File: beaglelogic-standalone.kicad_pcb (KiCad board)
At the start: 4 copper layers, 247 parts, among them J1 USB_OTG, J2 CONN_02X02, J3 USB_A, J4 CONN_01X06, J5 SI-51009-F, J6 CONN_02X12, J7 CONN_02X16, Q1 BSS138, Q2 BSS138, SW1 SW_PUSH_SMALL_H, SW2 SW_PUSH_SMALL_H, U1 74LVC1G07, U10 MCP79410/TDFN, U11 SST26VF064B, U12 TPS73101, U13 SN74LVCH16T245, U14 DVIULC6-4SC6, U15 DVIULC6-4SC6, U16 DVIULC6-4SC6, U17 DVIULC6-4SC6, U18 74LV1T125, U19 EMMC_4G, U2 AP1117, U3 TPS2051C, U4 TPD4S012, U5 TPD4S012, U6 OSD3358-SM, U7 KSZ9031RNXCC, U8 74LVC2G241, U9 74LVC1G125, Y1 25MHz, Y2 24MHz, Y3 32.768kHz,CL=9pF

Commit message: More routing
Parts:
- C44, C45, C46, C47, C48, C49, C50, C51, C54, C55, C56, C57, C58, C59, C60, C61, R103, R104, R105, R106, R107, R108, R109, R110, R111, R112, R113, R114, R115, R116, R117, R118, R119, R120, R121, R122, R123, R124, R125, R126, R42, R43, R65, R66, R67, R68, R69, R70, R71, R72, R73, R74, R75, R76, R77, R78, R79, R80, R87, R88, R89, R90, R91, R92, R93, R94, TP2, TP4, TP5, U13, U14, U15, U16, U17, U5: moved to B.Cu
- JP1, R46: moved to F.Cu
- moved R46 56.0 mm to (65.6, 147.6), turned to 270 degrees
- moved R45 54.1 mm to (57.5, 150.9), turned to 180 degrees
- moved R44 51.5 mm to (57.5, 149.7)
- moved JP1 51.2 mm to (54.1, 144.8)
- moved C36 50.7 mm to (58.0, 143.5)
- moved U11 49.1 mm to (65.0, 143.8), turned to 180 degrees
- moved C38 48.0 mm to (64.7, 140.4)
- moved U9 47.0 mm to (63.4, 148.1)
- moved C34 40.6 mm to (114.5, 128.7)
- moved C35 40.6 mm to (114.5, 130.8)
- moved Y3 40.4 mm to (116.4, 129.7)
- moved C37 40.1 mm to (119.5, 128.2)
- moved R47 40.1 mm to (121.8, 129.7)
- moved U10 40.1 mm to (119.5, 130.5)
- moved BT1 37.9 mm to (116.1, 134.0), turned to 0 degrees
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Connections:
- RN1 pad 1: +3V3 -> Net-(RN1-Pad1)
- RN1 pad 2: +3V3 -> /PRU1_IN05
- RN1 pad 3: +3V3 -> /PRU1_IN04
- RN1 pad 4: +3V3 -> /PRU1_IN03
- RN1 pad 5: /PRU1_IN03 -> +3V3
- RN1 pad 6: /PRU1_IN04 -> +3V3
- RN1 pad 7: /PRU1_IN05 -> +3V3
- RN1 pad 8: Net-(RN1-Pad8) -> +3V3
- U13 pad 11: /DIN09 -> /DIN06
- U13 pad 12: /DIN08 -> /DIN07
- U13 pad 13: /DIN07 -> /DIN08
- U13 pad 14: /DIN06 -> /DIN09
- U13 pad 16: /DIN05 -> /DIN10
- U13 pad 17: /DIN04 -> /DIN11
- U13 pad 19: /DIN03 -> /DIN12
- U13 pad 2: /DIN15 -> /DIN00
- U13 pad 20: /DIN02 -> /DIN13
- U13 pad 22: /DIN01 -> /DIN14
- U13 pad 23: /DIN00 -> /DIN15
- U13 pad 26: /PRU1_IN00 -> /PRU1_IN15
- U13 pad 27: /PRU1_IN01 -> /PRU1_IN14
- U13 pad 29: /PRU1_IN02 -> /PRU1_IN13
- U13 pad 3: /DIN14 -> /DIN01
- U13 pad 30: /PRU1_IN03 -> /PRU1_IN12
- U13 pad 32: /PRU1_IN04 -> /PRU1_IN11
- U13 pad 33: /PRU1_IN05 -> /PRU1_IN10
- U13 pad 35: /PRU1_IN06 -> /PRU1_IN09
- U13 pad 36: /PRU1_IN07 -> /PRU1_IN08
- U13 pad 37: /PRU1_IN08 -> /PRU1_IN07
- U13 pad 38: /PRU1_IN09 -> /PRU1_IN06
- U13 pad 40: /PRU1_IN10 -> /PRU1_IN05
- U13 pad 41: /PRU1_IN11 -> /PRU1_IN04
- U13 pad 43: /PRU1_IN12 -> /PRU1_IN03
- U13 pad 44: /PRU1_IN13 -> /PRU1_IN02
- U13 pad 46: /PRU1_IN14 -> /PRU1_IN01
- U13 pad 47: /PRU1_IN15 -> /PRU1_IN00
- U13 pad 5: /DIN13 -> /DIN02
- U13 pad 6: /DIN12 -> /DIN03
- U13 pad 8: /DIN11 -> /DIN04
- U13 pad 9: /DIN10 -> /DIN05
- U6 pad L1: Net-(RN1-Pad8) -> Net-(RN1-Pad1)
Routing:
- net /TRD4+: track 16.0 -> 0.00 mm
- net /TRD4-: track 15.9 -> 0.00 mm
- net USB0_D+: track 36.9 -> 21.1 mm
- net /TRD3+: track 14.7 -> 0.00 mm
- net /TRD3-: track 14.6 -> 0.00 mm
- net /TRD1+: track 14.5 -> 0.00 mm
- net /TRD1-: track 14.5 -> 0.00 mm
- net /TRD2+: track 13.9 -> 0.00 mm
- net /TRD2-: track 13.9 -> 0.00 mm
- net Net-(C11-Pad1): track 0.00 -> 13.3 mm, vias 0 -> 3
- net Net-(C12-Pad1): track 18.3 -> 28.6 mm, vias 5 -> 6
- net USB1_D-: track 30.7 -> 20.6 mm
- net USB1_D+: track 32.2 -> 22.2 mm
- net USB0_D-: track 36.9 -> 27.0 mm
- net Net-(C25-Pad1): track 0.00 -> 7.80 mm
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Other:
- board outline added: 106.4 x 66.1 mm

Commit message: Update routing and schematic
Signed-off-by: Kumar Abhishek <abhishek@theembeddedkitchen.net>
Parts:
- removed TP1: 5V, Measurement_Points:Measurement_Point_Round-SMD-Pad_Small
- added J8: Barrel_Jack, Connect:BARREL_JACK, F.Cu at (103.2, 123.9)
- added LOGO1: TEST_1P, beaglelogic-standalone:beaglelogic-logo, F.Cu at (106.6, 132.6)
- added M1: TEST_1P, Mounting_Holes:MountingHole_3.2mm_M3, F.Cu at (22.0, 166.4)
- added M2: TEST_1P, Mounting_Holes:MountingHole_3.2mm_M3, F.Cu at (123.1, 165.4)
- added M3: TEST_1P, Mounting_Holes:MountingHole_3.2mm_M3, F.Cu at (23.5, 106.7)
- added M4: TEST_1P, Mounting_Holes:MountingHole_3.2mm_M3, F.Cu at (120.9, 108.2)
- C40, C41, U14, U15, U16, U17: moved to F.Cu
- C43, C52, R81, R82, R95, U18: moved to B.Cu
- moved Y3 91.0 mm to (31.1, 161.5)
- moved BT1 91.0 mm to (30.8, 165.8)
- moved C34 91.0 mm to (29.2, 160.4)
- moved C35 91.0 mm to (29.2, 162.6)
- moved C37 91.0 mm to (34.2, 160.0)
- moved R47 91.0 mm to (36.5, 161.5)
- moved U10 91.0 mm to (34.2, 162.3)
- moved C41 16.6 mm to (24.3, 160.6), turned to 270 degrees
- moved C40 16.2 mm to (25.6, 160.7), turned to 270 degrees
- moved Q1 15.3 mm to (108.1, 139.9)
- moved C39 11.1 mm to (91.0, 141.5)
- moved R53 10.8 mm to (39.9, 154.7)
- moved U14 10.1 mm to (106.7, 143.6)
- moved C2 10.1 mm to (39.5, 113.2)
- moved C28 10.1 mm to (38.1, 120.7)
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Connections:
- net Net-(TP1-Pad1) renamed 5V_IN
- J6 pad 5: /UART1_RXD -> /UART1_TXD
- J6 pad 6: /UART1_TXD -> /UART1_RXD
- J6 pad 7: /I2C2_SCL -> /I2C2_SDA
- J6 pad 8: /I2C2_SDA -> /I2C2_SCL
- RN1 pad 1: Net-(RN1-Pad1) -> +3V3
- RN1 pad 2: /PRU1_IN05 -> +3V3
- RN1 pad 3: /PRU1_IN04 -> +3V3
- RN1 pad 4: /PRU1_IN03 -> +3V3
- RN1 pad 5: +3V3 -> Net-(RN1-Pad5)
- RN1 pad 6: +3V3 -> /PRU1_IN05
- RN1 pad 7: +3V3 -> /PRU1_IN04
- RN1 pad 8: +3V3 -> /PRU1_IN03
- U6 pad L1: Net-(RN1-Pad1) -> Net-(RN1-Pad5)
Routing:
- net GND: track 32.1 -> 91.3 mm, vias 0 -> 5
- net /GPIO3_17: track 0.00 -> 28.4 mm
- net /GPIO3_21: track 0.00 -> 26.9 mm
- net /SPI1_MISO: track 0.76 -> 26.6 mm
- net +3V3: track 0.00 -> 25.8 mm, vias 0 -> 1
- net /UART1_RXD: track 0.00 -> 24.3 mm
- net /GPIO3_16: track 0.00 -> 24.3 mm
- net /UART1_TXD: track 0.00 -> 23.6 mm
- net /I2C2_SCL: track 0.00 -> 22.9 mm
- net /I2C2_SDA: track 0.00 -> 21.6 mm
- net USB0_VBUS: track 0.00 -> 21.3 mm
- net /SPI1_SCK: track 0.79 -> 21.2 mm
- net /GPIO3_20: track 0.00 -> 20.3 mm
- net 3P3_AUX: track 0.00 -> 19.2 mm, vias 0 -> 2
- net /SPI1_MOSI: track 0.00 -> 18.9 mm, vias 0 -> 3
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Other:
- board size 106.4 x 66.1 mm -> 106.5 x 66.1 mm
- copper layers 4 -> 6

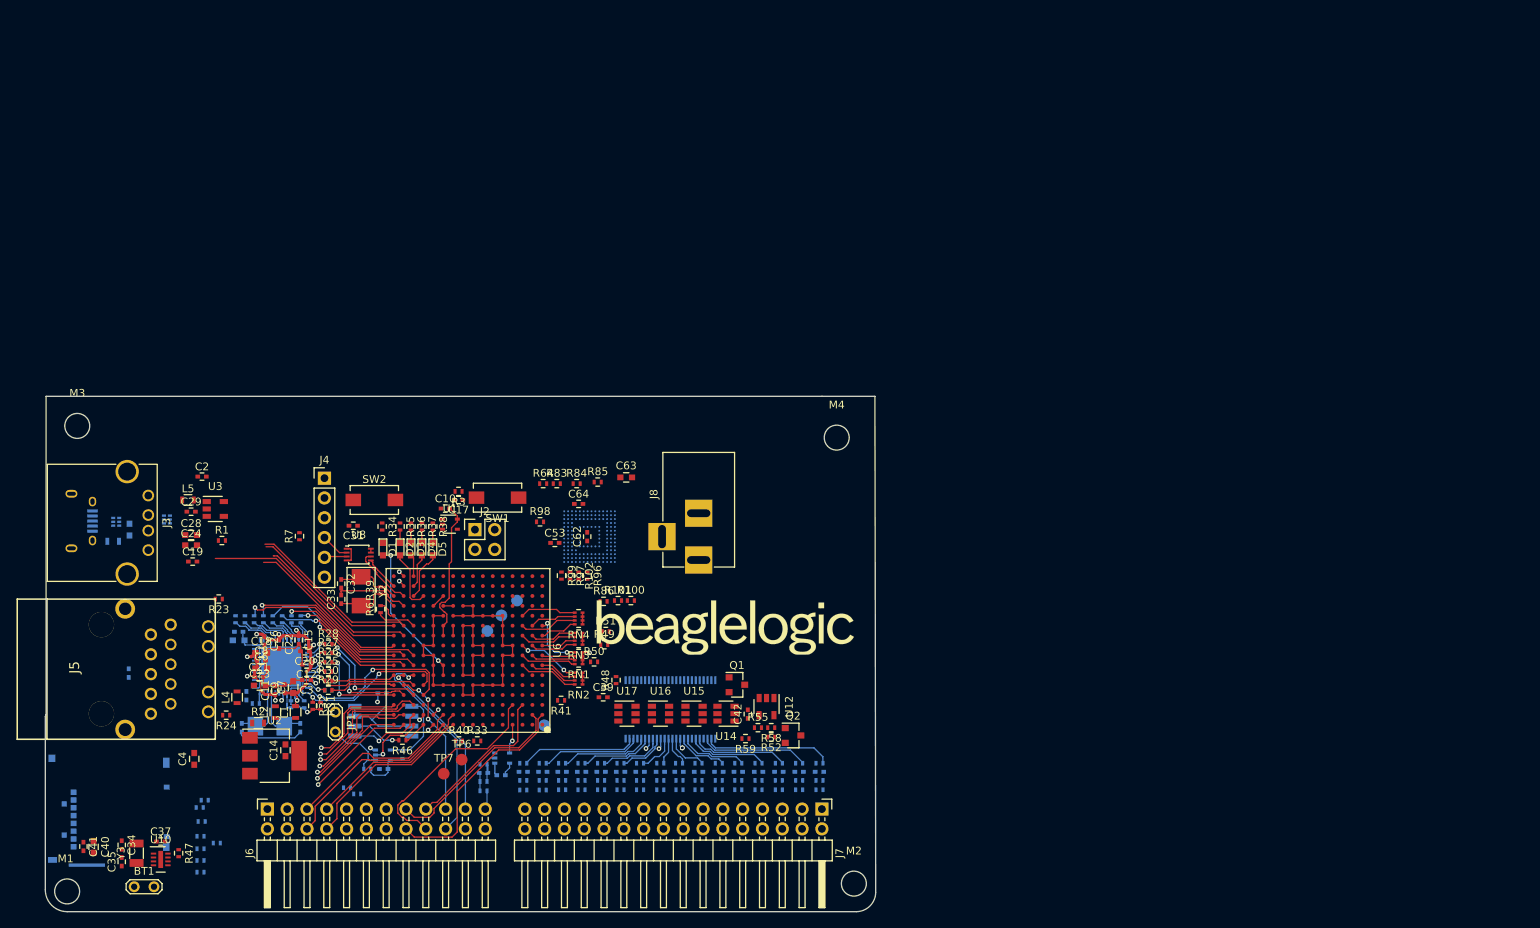
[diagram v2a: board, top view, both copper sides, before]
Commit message: Finalize board outline to 10cm x 6cm
Signed-off-by: Kumar Abhishek <abhishek@theembeddedkitchen.net>
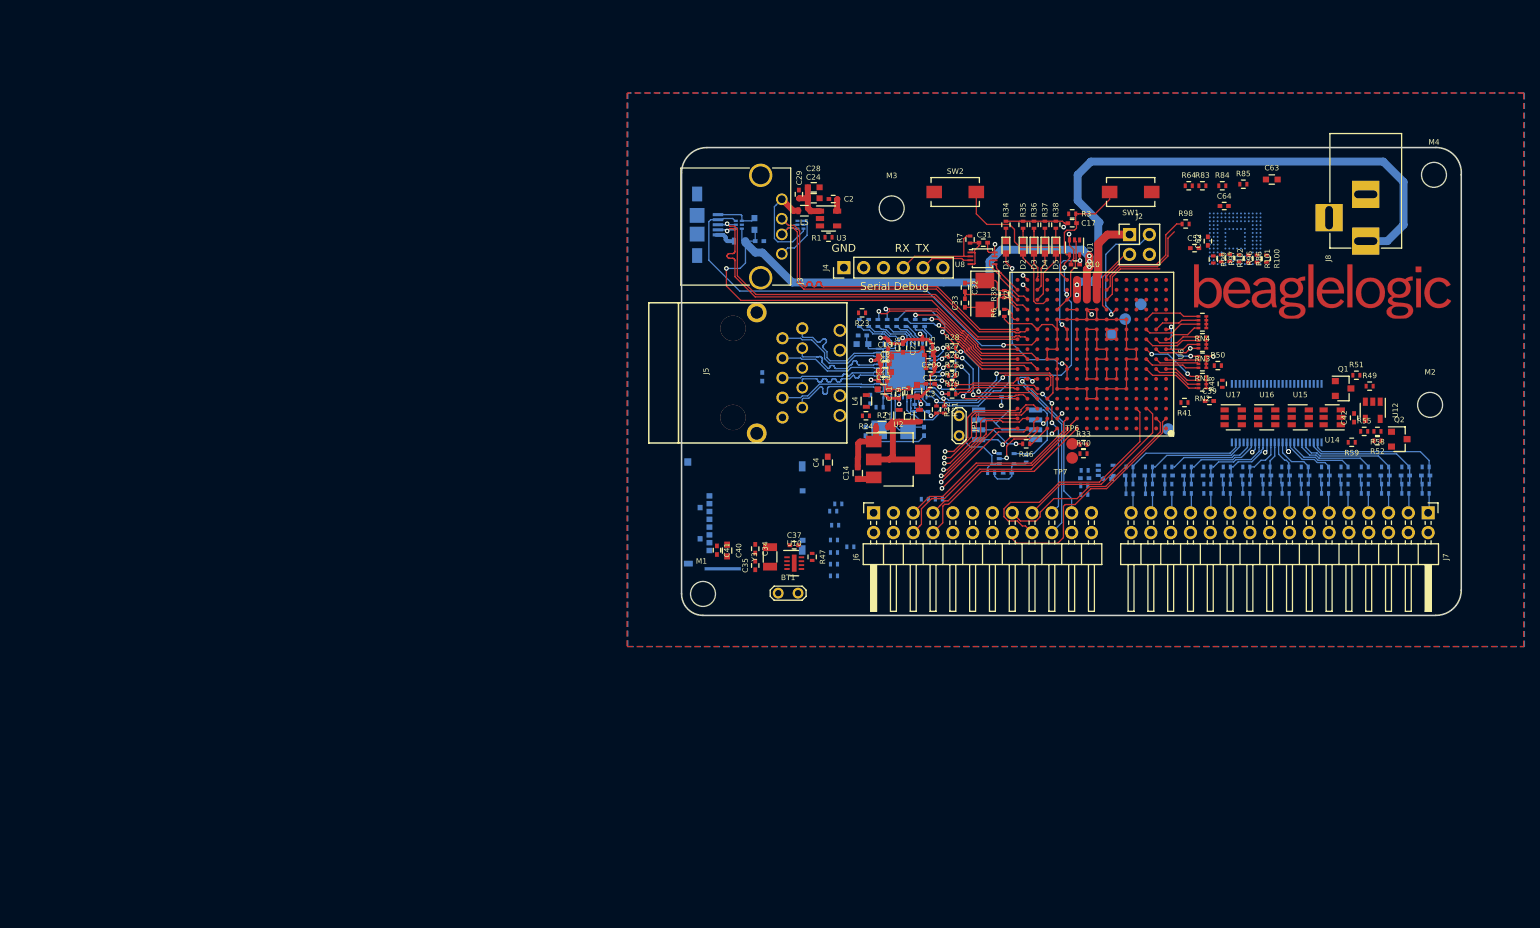
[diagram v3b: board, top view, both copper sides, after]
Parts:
- C19: moved to B.Cu
- J1: footprint Connect:USB_Micro-B -> beaglelogic-standalone:USB_MICRO_B_ST-USB-001E
- moved M3 108.1 mm to (128.0, 78.8)
- moved R49 103.6 mm to (189.2, 101.6)
- moved R51 101.7 mm to (187.6, 100.2)
- moved M2 96.1 mm to (197.0, 104.0)
- moved J8 94.8 mm to (188.8, 83.0)
- moved R7 94.0 mm to (138.0, 82.8)
- moved R86 93.7 mm to (173.7, 85.2), turned to 270 degrees
- moved R96 93.0 mm to (172.5, 85.2)
- moved R101 92.9 mm to (174.8, 85.2), turned to 270 degrees
- moved R99 92.9 mm to (169.2, 85.3)
- moved R102 92.9 mm to (171.3, 85.2)
- moved R97 92.9 mm to (170.2, 85.2)
- moved R100 92.5 mm to (176.0, 85.2), turned to 270 degrees
- moved J2 92.1 mm to (158.5, 82.2)
- moved C28 91.5 mm to (118.0, 76.1)
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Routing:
- net USB0_VBUS: track 21.3 -> 111.2 mm, vias 0 -> 4
- net 5V_IN: track 0.00 -> 76.0 mm, vias 0 -> 2
- net USB0_ID: track 0.00 -> 55.7 mm, vias 0 -> 1
- net SYS_RESETn: track 1.04 -> 55.4 mm, vias 1 -> 2
- net GND: track 91.3 -> 132.5 mm, vias 5 -> 8
- net USB0_D+: track 21.0 -> 50.8 mm, vias 0 -> 1
- net USB0_D-: track 27.0 -> 50.8 mm, vias 0 -> 1
- net USB1_D-: track 20.6 -> 43.8 mm
- net USB1_D+: track 22.1 -> 43.8 mm
- net Net-(SW2-Pad2): track 0.00 -> 20.7 mm
- net Net-(C4-Pad1): track 0.00 -> 15.7 mm
- net TS: track 0.00 -> 15.6 mm, vias 0 -> 1
- net /TRD4+: track 0.00 -> 14.5 mm
- net /TRD4-: track 0.00 -> 14.5 mm
- net /EMMC_CLK: track 0.00 -> 14.5 mm
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- added copper zone on In3.Cu, net +3V3
- added copper zone on B.Cu, net GND
- added copper zone on F.Cu, net GND
- added copper zone on In2.Cu, net GND
- added copper zone on In4.Cu, net GND
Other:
- board size 106.5 x 66.1 mm -> 100 x 60 mm
- board text added: "GND"
- board text added: "RX"
- board text added: "Serial Debug"
- board text added: "TX"

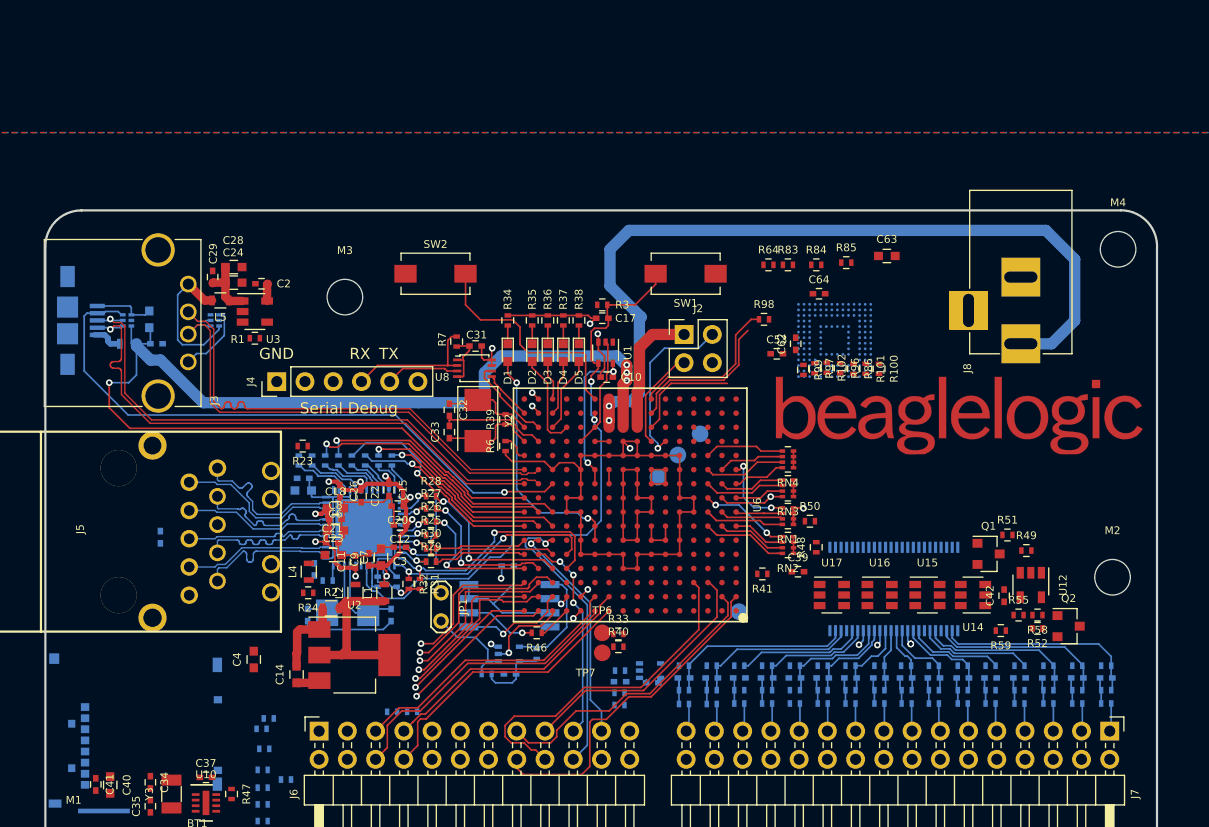
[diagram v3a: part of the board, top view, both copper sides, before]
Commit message: Route the eMMC
Signed-off-by: Kumar Abhishek <abhishek@theembeddedkitchen.net>
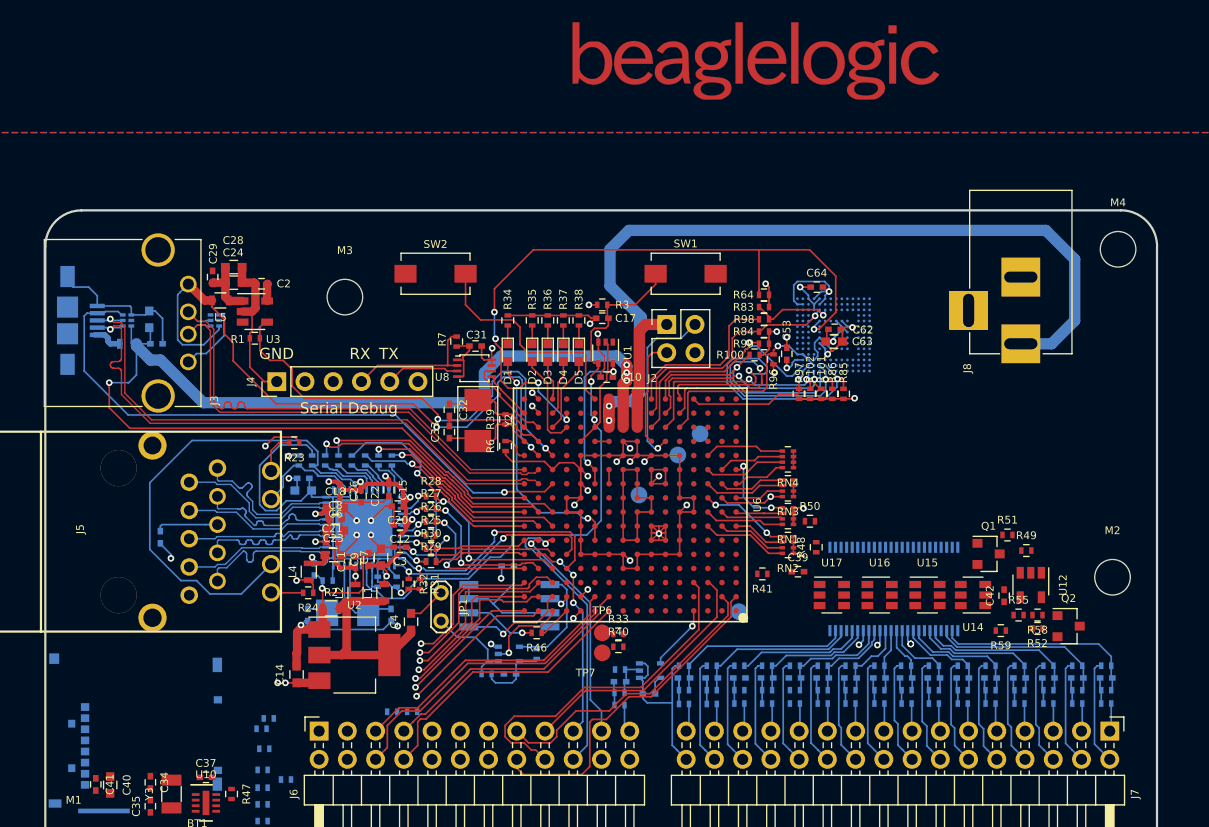
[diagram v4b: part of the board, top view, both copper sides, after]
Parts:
- moved LOGO1 36.8 mm to (164.9, 57.6)
- moved C4 14.6 mm to (133.9, 108.0)
- moved R85 11.8 mm to (172.8, 87.5), turned to 270 degrees
- moved R100 11.3 mm to (164.8, 84.0), turned to 0 degrees
- moved C63 9.05 mm to (171.9, 82.8), turned to 180 degrees
- moved R84 7.62 mm to (165.7, 81.9)
- moved R96 6.05 mm to (166.5, 84.4)
- moved R101 4.59 mm to (170.8, 87.5)
- moved R83 4.37 mm to (165.7, 79.7)
- moved R99 4.26 mm to (165.7, 83.0), turned to 0 degrees
- moved C62 3.73 mm to (172.0, 81.7), turned to 180 degrees
- moved R86 2.94 mm to (171.8, 87.5)
- moved R102 2.79 mm to (169.8, 87.5)
- moved R64 2.73 mm to (165.7, 78.6)
- moved R97 2.69 mm to (168.8, 87.5)
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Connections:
- U19 pad A1: (no net) -> /EMMC_DAT3
- U19 pad A2: (no net) -> /EMMC_DAT4
- U19 pad A6: (no net) -> /EMMC_DAT6
- U19 pad A7: (no net) -> /EMMC_DAT7
- U19 pad N1: (no net) -> GND
- U6 pad R13: /EMMC_RESETn -> /EMMC_RSTn
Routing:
- net GND: track 132.5 -> 371.4 mm, vias 8 -> 30
- net /EMMC_RSTn: track 0.00 -> 61.3 mm, vias 0 -> 5
- net USB1_VBUS: track 12.9 -> 57.8 mm, vias 0 -> 2
- net USB1_DRVVBUS: track 0.00 -> 41.4 mm, vias 0 -> 2
- net +3V3: track 33.1 -> 73.9 mm, vias 2 -> 15
- net Net-(J5-Pad14): track 5.11 -> 43.6 mm
- net /EMMC_DAT7: track 0.00 -> 32.4 mm, vias 0 -> 2
- net /EMMC_DAT6: track 0.00 -> 29.1 mm, vias 0 -> 2
- net /ETH_3V3: track 31.4 -> 55.7 mm, vias 2 -> 3
- net /EMMC_DAT2: track 0.00 -> 21.5 mm, vias 0 -> 1
- net /EMMC_DAT5: track 0.00 -> 19.8 mm, vias 0 -> 1
- net /EMMC_DAT1: track 0.00 -> 19.7 mm, vias 0 -> 2
- net /EMMC_DAT0: track 0.00 -> 19.2 mm, vias 0 -> 2
- net /EMMC_DAT4: track 0.00 -> 12.9 mm, vias 0 -> 1
- net /EMMC_DAT3: track 9.74 -> 21.6 mm, vias 0 -> 1
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- added copper zone on In1.Cu, net GND

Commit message: Route the expansion header
Signed-off-by: Kumar Abhishek <abhishek@theembeddedkitchen.net>
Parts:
- moved C37 41.0 mm to (155.7, 114.2)
- moved U10 40.4 mm to (154.1, 112.4), turned to 90 degrees
- moved Y3 40.2 mm to (151.1, 112.8)
- moved C35 40.1 mm to (148.6, 112.1), turned to 180 degrees
- moved C34 39.7 mm to (148.6, 111.2), turned to 180 degrees
- moved R47 37.5 mm to (152.6, 109.6)
- moved BT1 34.9 mm to (145.4, 114.1)
- moved TP7 5.08 mm to (156.1, 109.9)
- moved TP6 3.32 mm to (154.3, 109.9)
- moved R33 1.56 mm to (151.0, 108.9)
- moved R40 1.56 mm to (151.0, 110.1)
- moved R41 0.36 mm to (165.3, 104.0)
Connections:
- U10 pad 9: (no net) -> GND
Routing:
- net /EHRPWM0B: track 0.00 -> 53.3 mm
- net /EHRPWM0A: track 0.00 -> 40.4 mm
- net /GPIO1_19: track 0.00 -> 36.8 mm, vias 0 -> 1
- net /EQEP0_B: track 0.00 -> 36.7 mm, vias 0 -> 3
- net /EQEP0_A: track 0.00 -> 32.5 mm, vias 0 -> 2
- net /GPIO1_18: track 0.00 -> 31.3 mm, vias 0 -> 1
- net /SPI1_CS0: track 0.00 -> 26.3 mm, vias 0 -> 2
- net /SPI1_CS1: track 0.00 -> 19.5 mm, vias 0 -> 1
- net Net-(BT1-Pad1): track 0.00 -> 10.9 mm
- net TRSTn: track 0.00 -> 4.58 mm
- net /GPIO3_21: track 30.9 -> 33.5 mm
- net /GPIO3_16: track 26.4 -> 28.3 mm
- net /GPIO3_20: track 23.2 -> 25.1 mm
- net /GPIO3_17: track 30.5 -> 32.1 mm
- net I2C0_SDA: track 0.00 -> 1.27 mm
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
